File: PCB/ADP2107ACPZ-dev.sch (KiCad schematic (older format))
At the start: 17 parts, among them P1 CONN_01X02, P2 CONN_01X02, U1 ADP2107

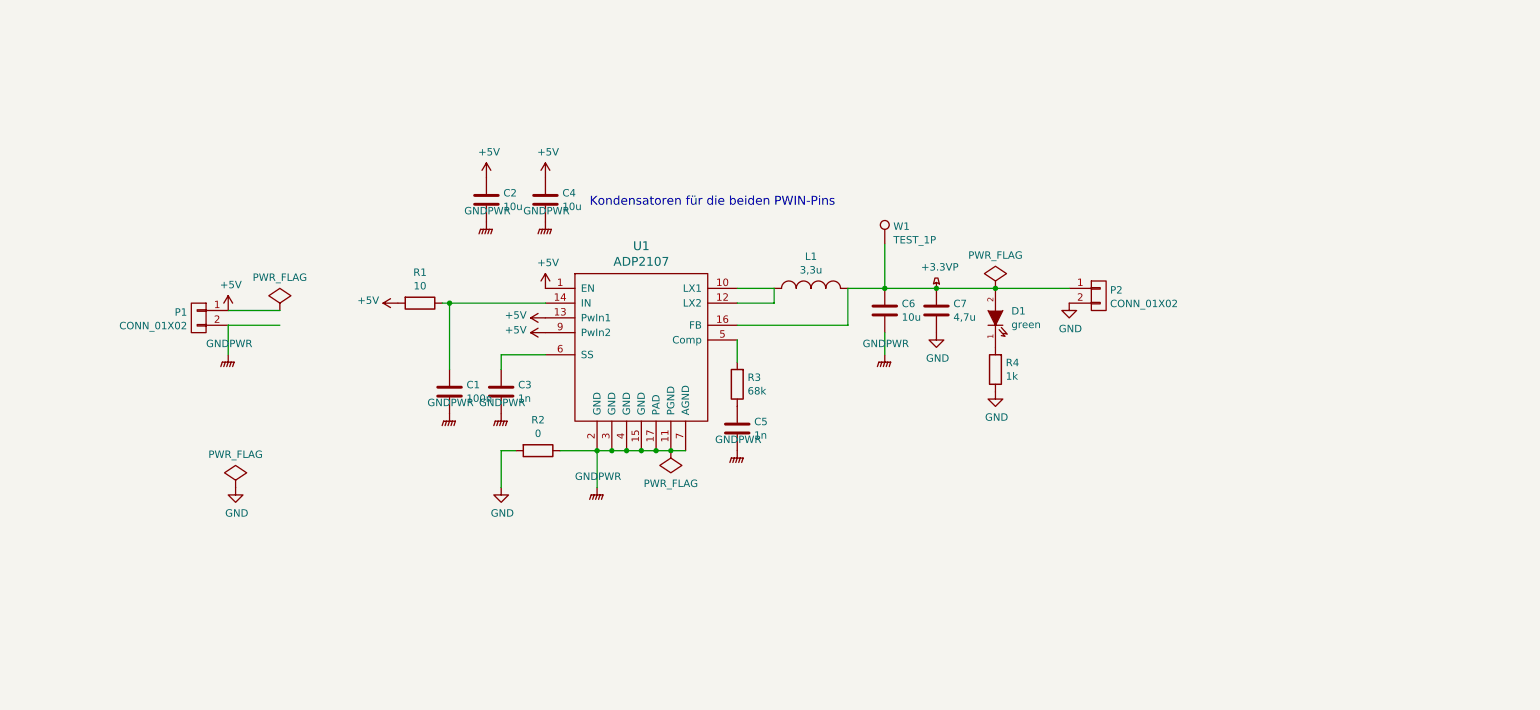
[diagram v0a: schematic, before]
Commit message: Datenblätter der Sende- und Verstärkerchips dazugefügt
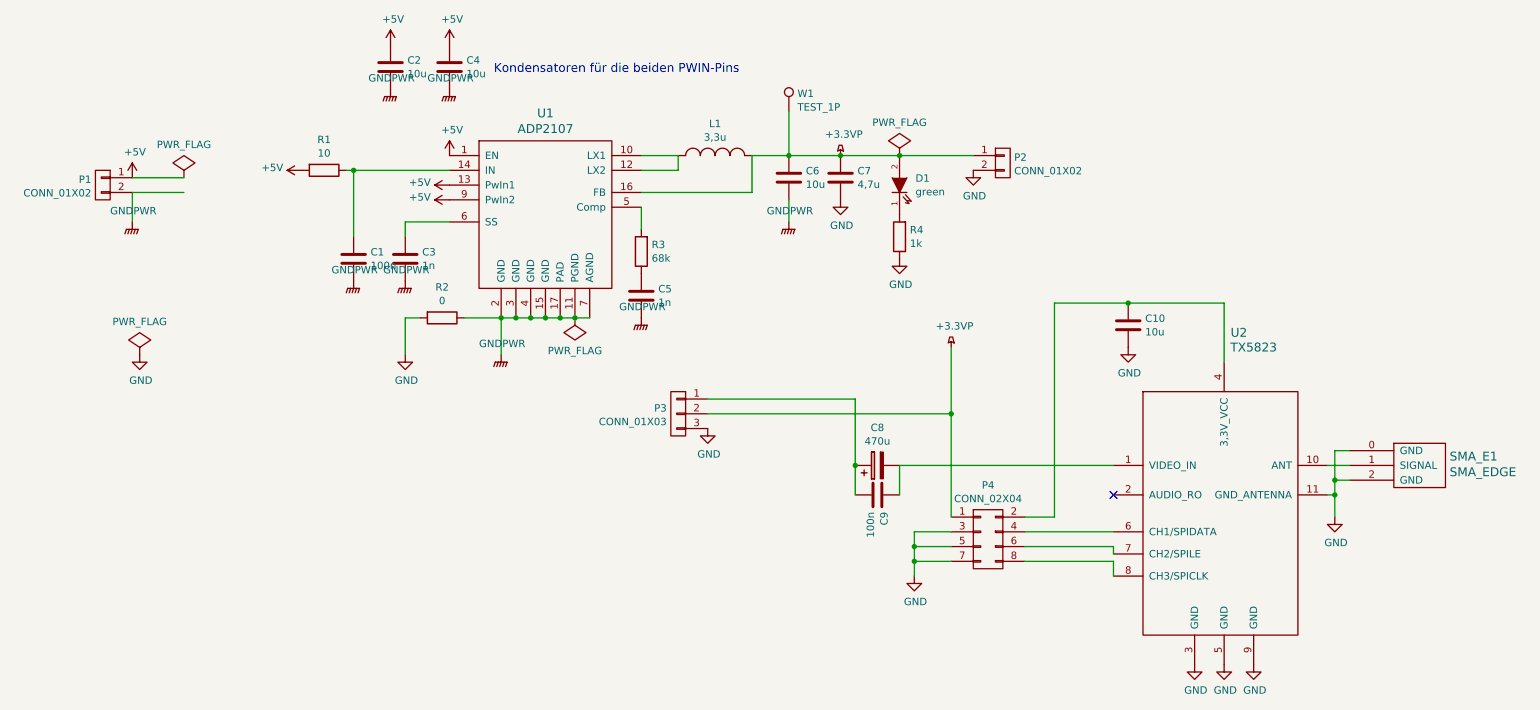
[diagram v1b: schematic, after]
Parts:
- added C10: 10u, Capacitors_SMD:C_0805, symbol C
- added C8: 470u, Capacitors_ThroughHole:C_Radial_D8_L13_P3.8, symbol CP
- added C9: 100n, Capacitors_SMD:C_0603, symbol C
- added P3: CONN_01X03, Pin_Headers:Pin_Header_Straight_1x03, symbol CONN_01X03
- added P4: CONN_02X04, Housings_DIP:DIP-8_W7.62mm_LongPads, symbol CONN_02X04
- added SMA_E1: SMA_EDGE, library_toni:SMA_EDGE, symbol SMA_EDGE
- added U2: TX5823, library_toni:TX5823, symbol TX5823
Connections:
- wire segments 20 -> 44
- no-connect marks 0 -> 1
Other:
- moved on the sheet: C1, C2, C3, C4, C5, C6, C7, D1, L1, P1, P2, R1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
